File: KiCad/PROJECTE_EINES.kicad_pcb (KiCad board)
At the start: 2 copper layers, 74.4 x 58.3 mm, 10 parts, among them J1 DE9_Pins_MountingHoles, J2 Conn_01x08_Pin, U1 LM1117DT-3.3, U3 VNH5019A-E, U4 LM2596S-5, U6 SN65HVD230

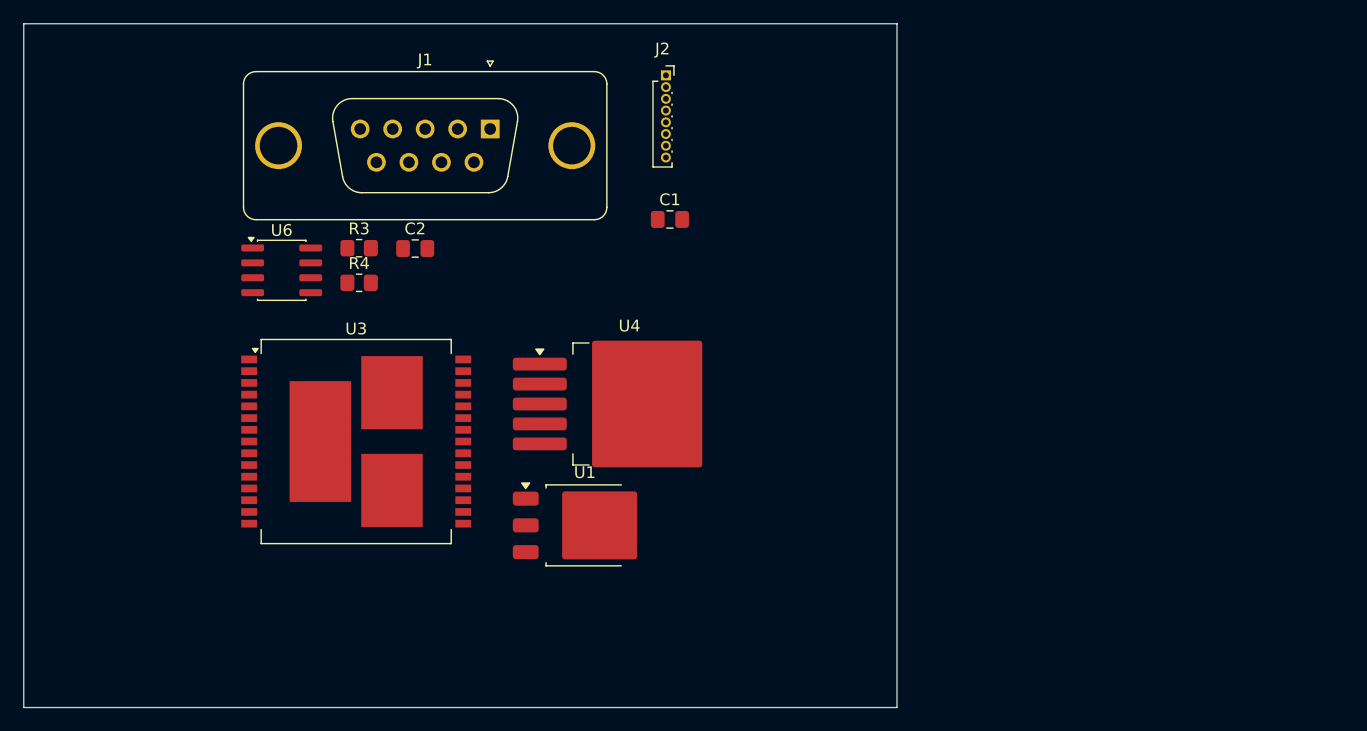
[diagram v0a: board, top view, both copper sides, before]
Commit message: Correció etapa d'alimentació e Inputs
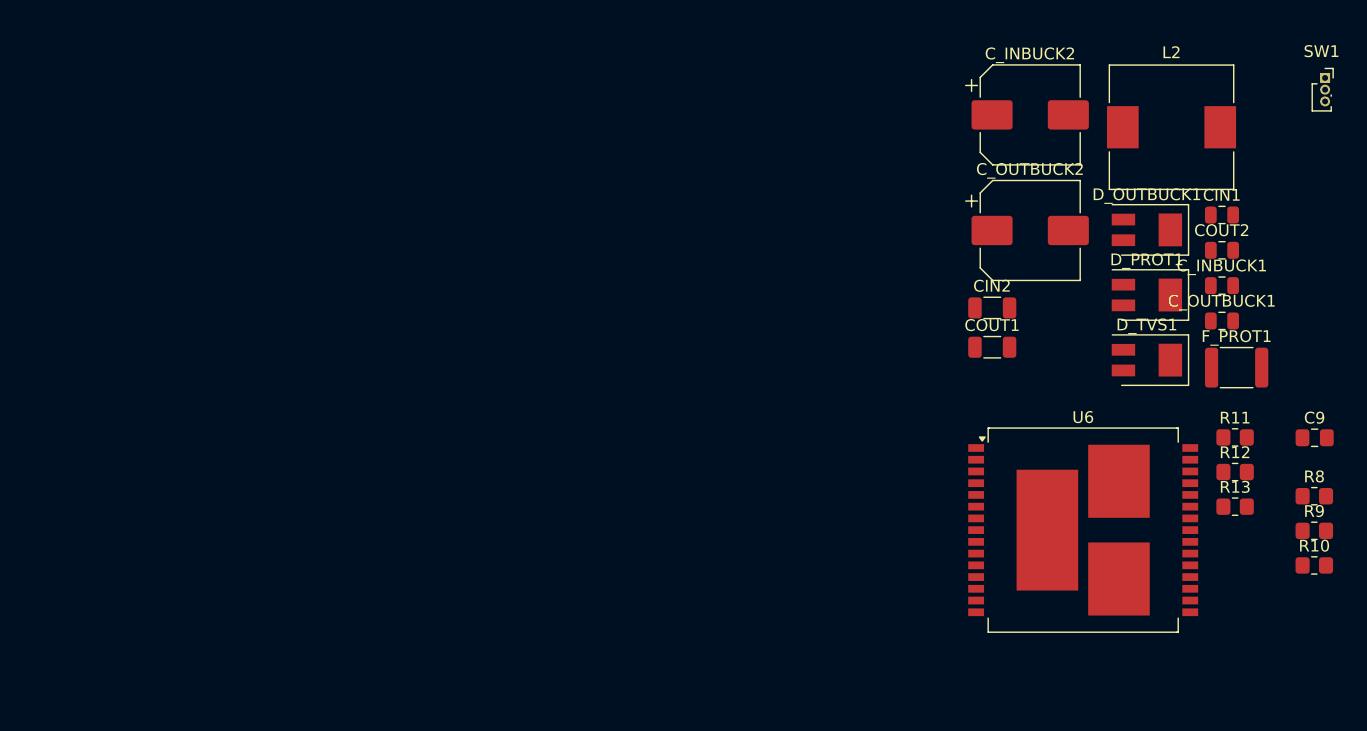
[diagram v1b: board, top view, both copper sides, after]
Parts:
- removed C1, C2: 100n, Capacitor_SMD:C_0805_2012Metric_Pad1.18x1.45mm_HandSolder
- removed J1: DE9_Pins_MountingHoles, Connector_Dsub:DSUB-9_Socket_Vertical_P2.77x2.84mm_MountingHoles
- removed J2: Conn_01x08_Pin, Connector_PinSocket_1.00mm:PinSocket_1x08_P1.00mm_Vertical
- removed R3: 10k, Resistor_SMD:R_0805_2012Metric_Pad1.20x1.40mm_HandSolder
- removed R4: 120, Resistor_SMD:R_0805_2012Metric_Pad1.20x1.40mm_HandSolder
- removed U1: LM1117DT-3.3, Package_TO_SOT_SMD:TO-252-3_TabPin2
- removed U3: VNH5019A-E, Package_SO:ST_MultiPowerSO-30
- removed U4: LM2596S-5, Package_TO_SOT_SMD:TO-263-5_TabPin3
- added C9: 100n, Capacitor_SMD:C_0805_2012Metric_Pad1.18x1.45mm_HandSolder, F.Cu at (230.5, 80.4)
- added CIN1: 100nF, Capacitor_SMD:C_0805_2012Metric, F.Cu at (222.6, 61.4)
- added CIN2: 10uF, Capacitor_SMD:C_1206_3216Metric, F.Cu at (203.0, 69.3)
- added COUT1: 10uF, Capacitor_SMD:C_1206_3216Metric, F.Cu at (203.0, 72.7)
- added COUT2: 100nF, Capacitor_SMD:C_0805_2012Metric, F.Cu at (222.6, 64.4)
- added C_INBUCK1: 100nF, Capacitor_SMD:C_0805_2012Metric, F.Cu at (222.6, 67.4)
- added C_INBUCK2: 220uF, Capacitor_SMD:CP_Elec_8x10, F.Cu at (206.2, 52.9)
- added C_OUTBUCK1: 100nF, Capacitor_SMD:C_0805_2012Metric, F.Cu at (222.6, 70.4)
- added C_OUTBUCK2: 220uF, Capacitor_SMD:CP_Elec_8x10, F.Cu at (206.2, 62.7)
- added D_OUTBUCK1: D_Schottky, Diode_SMD:D_SMB_Modified, F.Cu at (216.2, 62.6)
- added D_PROT1: D_Schottky, Diode_SMD:D_SMB_Modified, F.Cu at (216.2, 68.2)
- added D_TVS1: D_TVS, Diode_SMD:D_SMB_Modified, F.Cu at (216.2, 73.8)
- added F_PROT1: Fuse, Fuse:Fuse_1812_4532Metric, F.Cu at (223.8, 74.4)
- added L2: 33uH, Inductor_SMD:L_10.4x10.4_H4.8, F.Cu at (218.3, 53.9)
- added R10: 3.3k, Resistor_SMD:R_0805_2012Metric_Pad1.20x1.40mm_HandSolder, F.Cu at (230.5, 91.2)
- added R11: 1k, Resistor_SMD:R_0805_2012Metric_Pad1.20x1.40mm_HandSolder, F.Cu at (223.7, 80.3)
- added R12: 3.3k, Resistor_SMD:R_0805_2012Metric_Pad1.20x1.40mm_HandSolder, F.Cu at (223.7, 83.3)
- added R13: 3.3k, Resistor_SMD:R_0805_2012Metric_Pad1.20x1.40mm_HandSolder, F.Cu at (223.7, 86.2)
- added R8: 1,5K, Resistor_SMD:R_0805_2012Metric_Pad1.20x1.40mm_HandSolder, F.Cu at (230.5, 85.3)
- added R9: 3.3k, Resistor_SMD:R_0805_2012Metric_Pad1.20x1.40mm_HandSolder, F.Cu at (230.5, 88.3)
- added SW1: SS-1GL2-F-D, Connector_PinSocket_1.00mm:PinSocket_1x03_P1.00mm_Vertical, F.Cu at (231.4, 49.7)
- U6: value SN65HVD230 -> VNH5019A-E; footprint Package_SO:SOIC-8_3.9x4.9mm_P1.27mm -> Package_SO:ST_MultiPowerSO-30
- moved U6 71.8 mm to (210.8, 88.2)
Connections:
- net /BUS CAN/CANRX renamed /DRIVER MOTOR PORTA/DOOR_INA
- U6 pad 1: /BUS CAN/CANTX -> DOOR_MOTOR_A
- U6 pad 2: GND_DIGITAL -> unconnected-(U6-NC-Pad2)
- U6 pad 3: VDD_3V3 -> VBAT_PROT
- U6 pad 5: unconnected-(U6-Vref-Pad5) -> /DRIVER MOTOR PORTA/DOOR_DIAGA
- U6 pad 6: /BUS CAN/CANL -> +3.3V
- U6 pad 7: /BUS CAN/CANH -> /DRIVER MOTOR PORTA/DOOR_PWM
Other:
- board outline removed

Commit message: Actualizació Footprints
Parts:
- removed R10, R9: 3.3k, Resistor_SMD:R_0805_2012Metric_Pad1.20x1.40mm_HandSolder
- removed R8: 1,5K, Resistor_SMD:R_0805_2012Metric_Pad1.20x1.40mm_HandSolder
- added C16: 100n, Capacitor_SMD:C_0805_2012Metric_Pad1.18x1.45mm_HandSolder, F.Cu at (181.0, 117.6)
- added C8: 100n, Capacitor_SMD:C_0805_2012Metric_Pad1.18x1.45mm_HandSolder, F.Cu at (162.8, 96.5)
- added C_WIN_1: 100nF, Capacitor_SMD:C_0805_2012Metric, F.Cu at (142.6, 90.3)
- added C_WIN_2: 10uF, Capacitor_SMD:C_1206_3216Metric, F.Cu at (122.1, 100.4)
- added C_WIN_CP1: 100nF, Capacitor_SMD:C_0805_2012Metric, F.Cu at (142.6, 93.3)
- added J2: DE9_Pins_MountingHoles, Connector_Dsub:DSUB-9_Socket_Vertical_P2.77x2.84mm_MountingHoles, F.Cu at (169.2, 86.3)
- added J3: Conn_01x08_Pin, Connector_PinSocket_1.00mm:PinSocket_1x08_P1.00mm_Vertical, F.Cu at (177.1, 105.4)
- added J_DEBUG1: Conn_01x05_Pin, Connector_PinHeader_2.54mm:PinHeader_1x05_P2.54mm_Vertical, F.Cu at (168.8, 47.8)
- added J_MOTOR_DOOR1: Conn_01x02_Pin, TerminalBlock:TerminalBlock_MaiXu_MX126-5.0-02P_1x02_P5.00mm, F.Cu at (158.0, 50.5)
- added J_MOTOR_WIN1: Conn_01x02_Pin, TerminalBlock:TerminalBlock_MaiXu_MX126-5.0-02P_1x02_P5.00mm, F.Cu at (158.0, 60.6)
- added J_PWR1: Conn_01x02_Pin, TerminalBlock:TerminalBlock_MaiXu_MX126-5.0-02P_1x02_P5.00mm, F.Cu at (158.0, 70.7)
- added R2: 10k, Resistor_SMD:R_0805_2012Metric_Pad1.20x1.40mm_HandSolder, F.Cu at (158.0, 96.5)
- added R3: 120, Resistor_SMD:R_0805_2012Metric_Pad1.20x1.40mm_HandSolder, F.Cu at (158.0, 99.4)
- added R_BTNDOWN1: 10K, Resistor_SMD:R_0805_2012Metric, F.Cu at (184.9, 47.0)
- added R_BTNUP1: 10K, Resistor_SMD:R_0805_2012Metric, F.Cu at (184.9, 49.9)
- added R_LIMIT1: 10K, Resistor_SMD:R_0805_2012Metric, F.Cu at (184.9, 52.9)
- added R_MCLR1: 10K, Resistor_SMD:R_0805_2012Metric, F.Cu at (184.9, 55.8)
- added R_WIN_CS1: 1,5K, Resistor_SMD:R_0805_2012Metric_Pad1.20x1.40mm_HandSolder, F.Cu at (142.8, 81.5)
- added R_WIN_DIAGA1: 3.3k, Resistor_SMD:R_0805_2012Metric_Pad1.20x1.40mm_HandSolder, F.Cu at (142.8, 84.4)
- added R_WIN_DIAGB1: 3.3k, Resistor_SMD:R_0805_2012Metric_Pad1.20x1.40mm_HandSolder, F.Cu at (142.8, 87.3)
- added SW_UP1: SW_MCLR, Button_Switch_SMD:SW_SPST_TL3342, F.Cu at (214.3, 72.5)
- added SW_UP2: SW_WINUP, Button_Switch_SMD:SW_SPST_TL3342, F.Cu at (175.1, 72.2)
- added SW_UP3: SW_WINDOWN, Button_Switch_SMD:SW_SPST_TL3342, F.Cu at (185.6, 72.0)
- added SW_UP4: SW_LIMIT, Button_Switch_SMD:SW_SPST_TL3342, F.Cu at (203.2, 72.5)
- added U1: LM2596S-5, Package_TO_SOT_SMD:TO-263-5_TabPin3, F.Cu at (141.8, 51.7)
- added U2: LM1117DT-3.3, Package_TO_SOT_SMD:TO-252-3_TabPin2, F.Cu at (146.4, 74.0)
- added U4: SN65HVD230, Package_SO:SOIC-8_3.9x4.9mm_P1.27mm, F.Cu at (151.4, 98.4)
- added U5: VNH5019A-E, Package_SO:ST_MultiPowerSO-30, F.Cu at (129.8, 89.3)
- added Y1: 8MHz, Crystal:Crystal_SMD_3225-4Pin_3.2x2.5mm, F.Cu at (121.9, 106.3)
- moved CIN1 101.2 mm to (121.5, 66.7)
- moved COUT2 101.2 mm to (121.5, 69.7)
- moved C_INBUCK1 101.2 mm to (121.5, 72.7)
- moved C_OUTBUCK1 101.2 mm to (121.5, 75.7)
- moved F_PROT1 96.9 mm to (127.2, 67.7)
- moved SW1 87.2 mm to (177.1, 117.9)
- moved C_INBUCK2 81.0 mm to (125.3, 50.4)
- moved C_OUTBUCK2 81.0 mm to (125.3, 60.3)
- moved D_OUTBUCK1 81.0 mm to (135.3, 60.6)
- moved D_PROT1 81.0 mm to (135.3, 66.2)
- moved D_TVS1 81.0 mm to (135.3, 71.7)
- moved CIN2 76.5 mm to (126.5, 71.8)
- moved COUT1 76.5 mm to (126.5, 75.2)
- moved L2 73.3 mm to (145.7, 63.8)
- moved R11 58.5 mm to (170.7, 105.1)
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
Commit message: 1ra versióPCB
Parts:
- removed C9: 100n, Capacitor_SMD:C_0805_2012Metric_Pad1.18x1.45mm_HandSolder
- removed C_WIN_1, C_WIN_CP1: 100nF, Capacitor_SMD:C_0805_2012Metric
- removed C_WIN_2: 10uF, Capacitor_SMD:C_1206_3216Metric
- removed J3: Conn_01x08_Pin, Connector_PinSocket_1.00mm:PinSocket_1x08_P1.00mm_Vertical
- removed L2: 33uH, Inductor_SMD:L_10.4x10.4_H4.8
- removed R11: 1k, Resistor_SMD:R_0805_2012Metric_Pad1.20x1.40mm_HandSolder
- removed R12, R13, R_WIN_DIAGA1, R_WIN_DIAGB1: 3.3k, Resistor_SMD:R_0805_2012Metric_Pad1.20x1.40mm_HandSolder
- removed R_WIN_CS1: 1,5K, Resistor_SMD:R_0805_2012Metric_Pad1.20x1.40mm_HandSolder
- removed U6: VNH5019A-E, Package_SO:ST_MultiPowerSO-30
- added C1: 100n, Capacitor_SMD:C_0805_2012Metric, F.Cu at (146.4, 55.9)
- added C_AVDD1: 100nF, Capacitor_SMD:C_0603_1608Metric, B.Cu at (101.9, 84.7)
- added C_BULK1: 10uF, Capacitor_SMD:C_0805_2012Metric, B.Cu at (104.7, 67.7)
- added C_CP_DOOR1: 100nF, Capacitor_SMD:C_0805_2012Metric, F.Cu at (68.6, 69.4)
- added C_OSC1: 22pF, Capacitor_SMD:C_0603_1608Metric, F.Cu at (118.8, 75.9)
- added C_OSC2: 22pF, Capacitor_SMD:C_0603_1608Metric, F.Cu at (118.8, 73.8)
- added C_VCAP1: 10uF, Capacitor_SMD:C_1206_3216Metric, B.Cu at (94.1, 77.5)
- added C_VDD1: 100nF, Capacitor_SMD:C_0603_1608Metric, B.Cu at (104.5, 85.4)
- added C_VDD2: 100nF, Capacitor_SMD:C_0603_1608Metric, B.Cu at (114.6, 84.6)
- added C_VDD_DOOR1: 100nF, Capacitor_SMD:C_0805_2012Metric, F.Cu at (43.8, 75.5)
- added C_VDD_DOOR2: 10uF, Capacitor_SMD:CP_Elec_8x10, F.Cu at (77.8, 83.4)
- added C_WIN_3: 100nF, Capacitor_SMD:C_0805_2012Metric, F.Cu at (67.5, 88.6)
- added C_WIN_4: 10uF, Capacitor_SMD:C_1206_3216Metric, F.Cu at (44.5, 99.8)
- added C_WIN_CP2: 100nF, Capacitor_SMD:C_0805_2012Metric, F.Cu at (73.4, 94.9)
- added J1: Conn_01x08_Pin, Connector_PinSocket_1.00mm:PinSocket_1x08_P1.00mm_Vertical, F.Cu at (143.0, 48.9)
- added L1: 33uH, Inductor_SMD:L_10.4x10.4_H4.8, F.Cu at (66.4, 36.2)
- added R1: 0, Resistor_SMD:R_0805_2012Metric, F.Cu at (106.4, 103.2)
- added R_BTNDOWN2: 10K, Resistor_SMD:R_0805_2012Metric, F.Cu at (149.6, 87.6)
- added R_BTNUP2: 10K, Resistor_SMD:R_0805_2012Metric, F.Cu at (145.4, 87.7)
- added R_CS_DOOR1: 1k, Resistor_SMD:R_0805_2012Metric, F.Cu at (69.3, 75.4)
- added R_DIAGA_DOOR1: 3.3k, Resistor_SMD:R_0805_2012Metric, F.Cu at (72.5, 78.2)
- added R_DIAGB_DOOR1: 3.3k, Resistor_SMD:R_0805_2012Metric, F.Cu at (72.0, 72.2)
- added R_LOCK1: 10K, Resistor_SMD:R_0805_2012Metric, F.Cu at (145.3, 94.3)
- added R_UNLOCK1: 10K, Resistor_SMD:R_0805_2012Metric, F.Cu at (149.7, 94.2)
- added R_WIN_CS2: 1,5K, Resistor_SMD:R_0805_2012Metric, F.Cu at (73.4, 100.9)
- added R_WIN_DIAGA2: 3.3k, Resistor_SMD:R_0805_2012Metric, F.Cu at (73.4, 103.9)
- added R_WIN_DIAGB2: 3.3k, Resistor_SMD:R_0805_2012Metric, F.Cu at (73.5, 98.2)
- added SW_UP5: SW_WINUP, Button_Switch_SMD:SW_SPST_TL3342, F.Cu at (138.4, 88.5)
- added SW_UP6: SW_WINDOWN, Button_Switch_SMD:SW_SPST_TL3342, F.Cu at (155.5, 88.0)
- added SW_UP7: SW_LIMIT, Button_Switch_SMD:SW_SPST_TL3342, F.Cu at (138.3, 97.4)
- added SW_UP8: SW_LIMIT, Button_Switch_SMD:SW_SPST_TL3342, F.Cu at (155.4, 96.8)
- added U3: LM2596S-5, Package_TO_SOT_SMD:TO-263-5_TabPin3, F.Cu at (51.7, 38.4)
- added U7: PIC24HJ128GP504-I_PT, PIC24HJ128GP504-I_PT:QFP80P1200X1200X120-44N, F.Cu at (104.5, 76.8)
- C16, C8: footprint Capacitor_SMD:C_0805_2012Metric_Pad1.18x1.45mm_HandSolder -> Capacitor_SMD:C_0805_2012Metric
- R2, R3: footprint Resistor_SMD:R_0805_2012Metric_Pad1.20x1.40mm_HandSolder -> Resistor_SMD:R_0805_2012Metric
- U1: value LM2596S-5 -> VNH5019A-E; footprint Package_TO_SOT_SMD:TO-263-5_TabPin3 -> Package_SO:ST_MultiPowerSO-30
- U2: value LM1117DT-3.3 -> VNH5019A-E; footprint Package_TO_SOT_SMD:TO-252-3_TabPin2 -> Package_SO:ST_MultiPowerSO-30
- U5: value VNH5019A-E -> LM1117DT-3.3; footprint Package_SO:ST_MultiPowerSO-30 -> Package_TO_SOT_SMD:TO-252-3_TabPin2
- moved J_PWR1 137.0 mm to (23.3, 46.0), turned to 90 degrees
- moved J_MOTOR_WIN1 126.7 mm to (36.9, 97.8), turned to -90 degrees
- moved J_MOTOR_DOOR1 124.6 mm to (36.6, 78.2), turned to 90 degrees
- moved D_PROT1 97.4 mm to (40.0, 46.2), turned to 180 degrees
- moved F_PROT1 96.9 mm to (32.7, 46.2)
- moved U1 96.2 mm to (58.4, 99.6), turned to 180 degrees
- moved D_TVS1 94.4 mm to (42.1, 56.1), turned to 90 degrees
- moved U2 89.5 mm to (56.9, 75.7), turned to 180 degrees
- moved J_DEBUG1 83.5 mm to (101.3, 96.9), turned to 90 degrees
- moved SW1 80.3 mm to (133.1, 50.8)
- moved C16 79.5 mm to (136.6, 51.8), turned to -90 degrees
- moved C_INBUCK1 75.7 mm to (47.8, 55.4), turned to -90 degrees
- moved SW_UP1 75.7 mm to (138.6, 70.2)
- moved D_OUTBUCK1 72.2 mm to (64.5, 46.5)
- moved J2 71.9 mm to (120.1, 33.8)
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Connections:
- net /BUS CAN/CANH renamed /COMUNICACIONS/CANH
- net /BUS CAN/CANL renamed /COMUNICACIONS/CANL
- net /INPUTS/WIN_BTN_DOWN renamed WIN_BTN_DOWN
- net /INPUTS/WIN_BTN_UP renamed WIN_BTN_UP
- C8 pad 2: +3.3V -> VDD_3V3
- COUT1 pad 1: +3.3V -> VDD_3V3
- COUT2 pad 1: +3.3V -> VDD_3V3
- J2 pad 9: RX -> UART_RX
- J_DEBUG1 pad 2: +3.3V -> VDD_3V3
- R_BTNDOWN1 pad 1: +3.3V -> VDD_3V3
- R_BTNUP1 pad 1: +3.3V -> VDD_3V3
- R_LIMIT1 pad 1: +3.3V -> VDD_3V3
- R_MCLR1 pad 1: +3.3V -> VDD_3V3
- R_MCLR1 pad 2: /INPUTS/MCLR -> MCLR
- SW_UP1 pad 1: /INPUTS/MCLR -> MCLR
- U1 pad 1: VBAT_PROT -> WIN_MOTOR_B
- U1 pad 2: Net-(D_OUTBUCK1-K) -> unconnected-(U1-NC-Pad2)
- U1 pad 3: GNDPWR -> VBAT_PROT
- U1 pad 4: +5V -> WIN_INA
- U1 pad 5: GNDPWR -> WIN_DIAGA
- U2 pad 1: GNDPWR -> DOOR_MOTOR_A
- U2 pad 2: +3.3V -> unconnected-(U2-NC-Pad2)
- U2 pad 3: +5V -> VBAT_PROT
- U4 pad 1: /BUS CAN/CANTX -> CAN_TX
- U4 pad 3: +3.3V -> VDD_3V3
- U4 pad 4: /BUS CAN/CANRX -> CAN_RX
- U5 pad 1: WIN_MOTOR_A -> GNDPWR
- U5 pad 2: unconnected-(U5-NC-Pad2) -> VDD_3V3
- U5 pad 3: VBAT_PROT -> +5V

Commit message: Versió 2.0 PCB
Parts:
- moved C8 53.9 mm to (167.4, 68.2)
- moved R_BTNDOWN1 53.9 mm to (201.7, 81.6)
- moved R_BTNDOWN2 53.9 mm to (202.1, 100.0)
- moved R_BTNUP2 53.9 mm to (197.9, 100.1)
- moved R_LOCK1 53.9 mm to (197.8, 106.7)
- moved R_MCLR1 53.9 mm to (197.5, 81.6)
- moved SW1 53.9 mm to (185.6, 63.1)
- moved SW_UP1 53.9 mm to (191.1, 82.6)
- moved SW_UP3 53.9 mm to (207.7, 82.7)
- moved SW_UP4 53.9 mm to (207.8, 91.4)
- moved SW_UP5 53.9 mm to (190.9, 100.9)
- moved SW_UP6 53.9 mm to (208.0, 100.4)
- moved CIN2 53.9 mm to (132.5, 49.6)
- moved COUT1 53.9 mm to (142.3, 59.7)
- moved C_CP_DOOR1 53.9 mm to (121.1, 81.8)
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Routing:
- net DOOR_INB: track 0.00 -> 21.8 mm
- net CAN_TX: track 0.00 -> 18.5 mm
- net MCLR: track 0.00 -> 12.6 mm
- net PGEC1: track 0.00 -> 10.6 mm
- net PGED1: track 0.00 -> 10.4 mm
- net Net-(U2-CP): track 0.00 -> 3.72 mm
- added copper zone on B.Cu, net GND
- added copper zone on F.Cu, net VDD_3V3
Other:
- board outline added: 157.7 x 100.2 mm

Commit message: Versió de placement PCB
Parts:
- removed C_BULK1: 10uF, Capacitor_SMD:C_0805_2012Metric
- C1: moved to B.Cu
- C_VDD_DOOR2: footprint Capacitor_SMD:CP_Elec_8x10 -> Capacitor_SMD:C_1206_3216Metric
- moved C16 114.9 mm to (104.7, 142.2)
- moved SW1 114.8 mm to (101.3, 141.1)
- moved J1 93.4 mm to (129.1, 127.1), turned to 90 degrees
- moved C1 77.8 mm to (123.0, 85.6), turned to 180 degrees
- moved SW_UP8 59.6 mm to (150.7, 126.3)
- moved R_UNLOCK1 58.7 mm to (145.0, 120.4), turned to 180 degrees
- moved R1 54.3 mm to (111.5, 142.1), turned to 0 degrees
- moved R_BTNDOWN2 49.7 mm to (155.1, 116.3)
- moved R_LOCK1 49.1 mm to (150.7, 120.4), turned to 0 degrees
- moved SW_UP6 48.7 mm to (162.3, 117.3)
- moved R_LIMIT1 48.1 mm to (154.9, 98.6), turned to 90 degrees
- moved R_BTNDOWN1 47.2 mm to (155.0, 89.0)
- moved SW_UP4 46.3 mm to (162.3, 99.9)
- moved SW_UP3 45.4 mm to (162.8, 90.2)
- moved J_DEBUG1 44.6 mm to (112.3, 127.2)
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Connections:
- C_CP_DOOR1 pad 1: GND -> GNDPWR
- C_VDD_DOOR1 pad 2: GND -> GNDPWR
- C_VDD_DOOR2 pad 2: GND -> GNDPWR
- C_WIN_3 pad 2: GND -> GNDPWR
- C_WIN_4 pad 2: GND -> GNDPWR
- C_WIN_CP2 pad 1: GND -> GNDPWR
- R_CS_DOOR1 pad 2: GND -> GNDPWR
- R_WIN_CS2 pad 2: GND -> GNDPWR
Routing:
- net DOOR_INB: track 21.8 -> 0.37 mm
- net CAN_TX: track 18.5 -> 0.00 mm
- net MCLR: track 12.6 -> 0.00 mm
- net PGEC1: track 10.6 -> 0.00 mm
- net PGED1: track 10.4 -> 0.00 mm
- net Net-(U2-CP): track 3.72 -> 0.43 mm
- net UART_RX: track 0.00 -> 1.22 mm
- removed copper zone on B.Cu, net GND
- removed copper zone on F.Cu, net VDD_3V3
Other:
- board size 157.7 x 100.2 mm -> 107 x 101.9 mm
